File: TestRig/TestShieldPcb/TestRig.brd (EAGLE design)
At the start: 53.3 x 61 mm, 7 parts, among them J1 POWER_JACKPTH, U1 ARDUINO_SHIELDNOHOLES

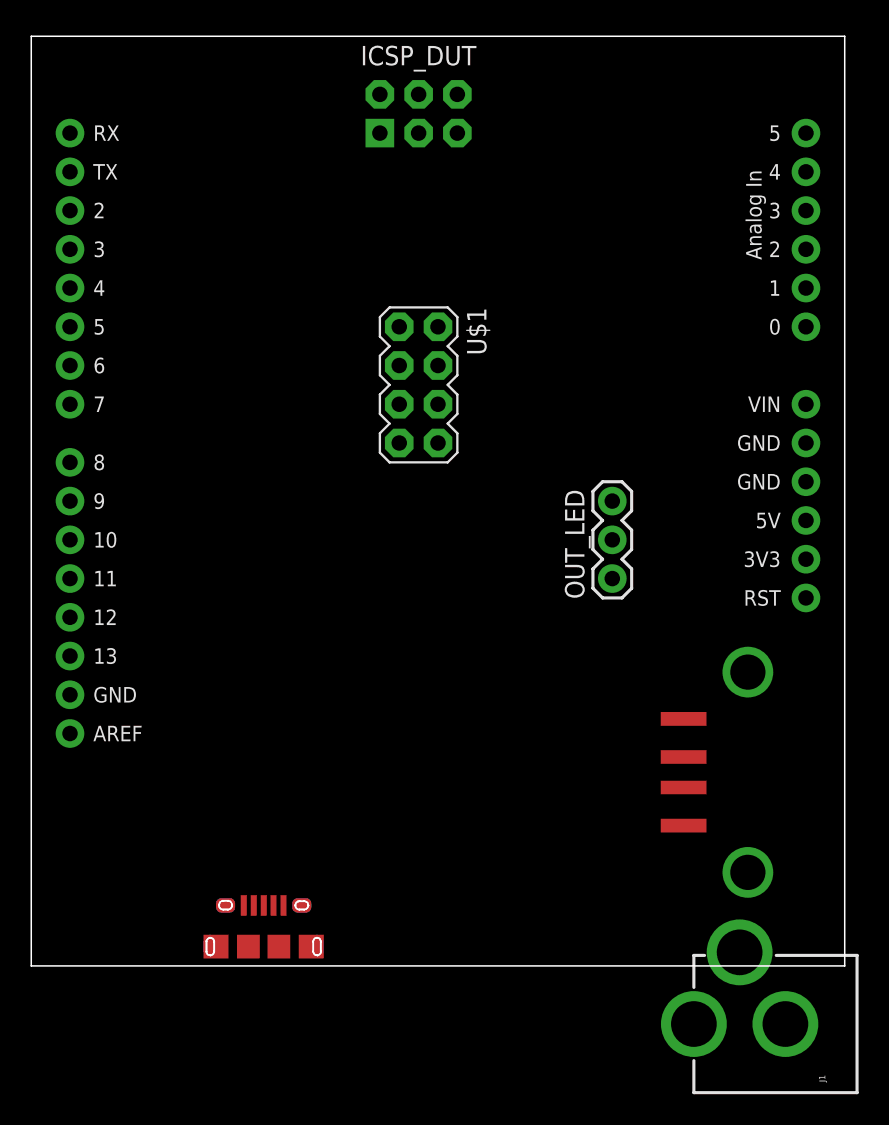
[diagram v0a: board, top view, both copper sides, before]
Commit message: Add test shield design
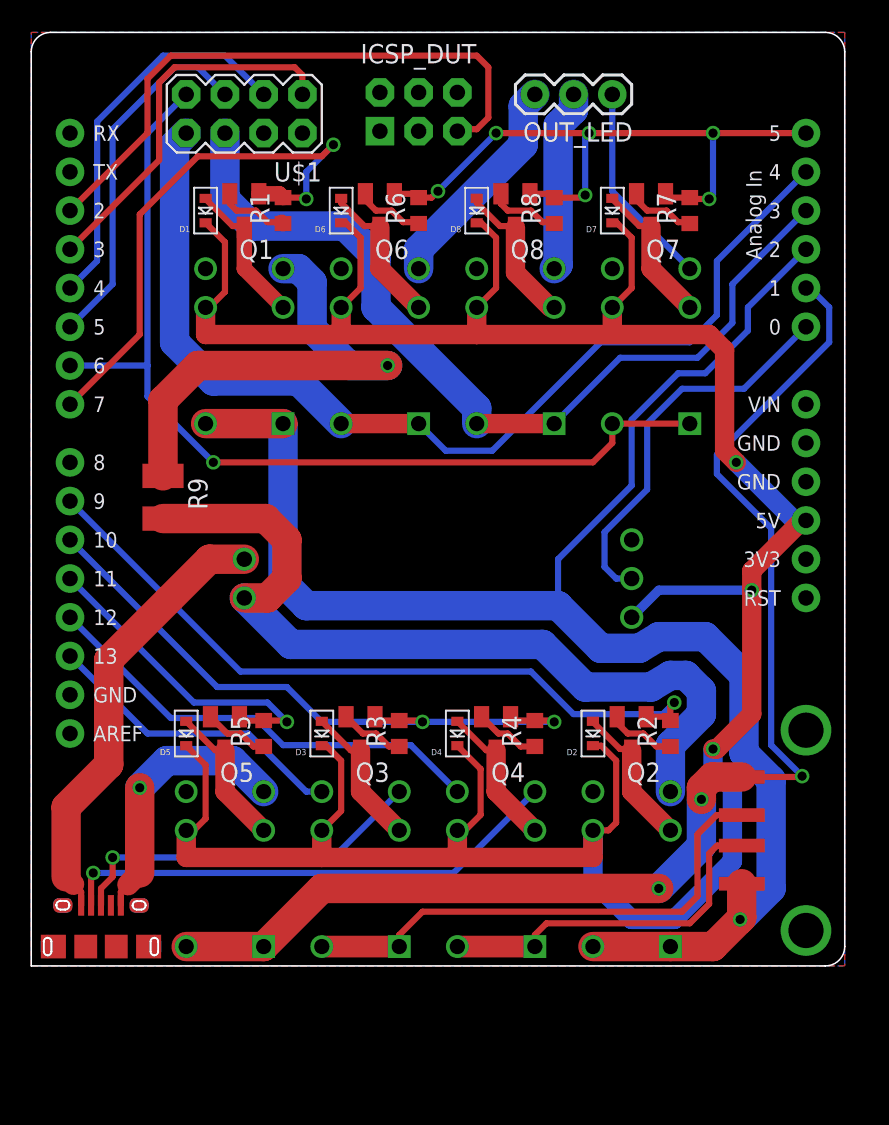
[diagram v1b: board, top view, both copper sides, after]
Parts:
- removed J1: POWER_JACKPTH, SparkFun-Connectors:POWER_JACK_PTH
- added D1, D2, D3, D4, D5, D6, D7, D8: (no value), adafruit:SOD-523
- added Q1, Q2, Q3, Q4, Q5, Q6, Q7, Q8: (no value), adafruit:SOT23
- added R1, R2, R3, R4, R5, R6, R7, R8: 1k, adafruit:R0603
- added R9: 25, adafruit:R1210
- added U$10, U$3, U$4, U$5, U$6, U$7, U$8, U$9: RELAY, blinkiverse:RELAY_HK23F-5V
- added U$11: SPARKFUN_ACS712, blinkiverse:SPARKFUN_ACS712
- moved OUT_LED 31.8 mm to (38.1, 57.1), turned to 180 degrees
- moved U$1 21.1 mm to (14.0, 55.9), turned to 180 degrees
- moved U$2 10.7 mm to (4.57, 1.27)
- moved JP1 5.39 mm to (50.8, 8.89)
- moved ICSP_DUT 0.13 mm to (25.4, 56.0)
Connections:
- net DUT_GND_IN renamed DUT_IN_GND_NC
- net DUT_VCC_IN renamed DUT_IN_VCC_NC
- removed net DUT_5V_OUT: U$1.6
- removed net DUT_GND_OUT: U$1.8
- removed net DUT_USB_V+: JP1.VBUS, U1.D12
- removed net N$1: U1.D4
- removed net N$10: U1.D9
- removed net N$2: U1.D5
- removed net N$7: U1.D6
- removed net N$8: U1.D7
- new net 5V: D1.K, D2.K, D3.K, D4.K, D5.K, D6.K, D7.K, D8.K, U$10.P$5, U$11.5V, U$3.P$5, U$4.P$5, U$5.P$5, U$6.P$5, U$7.P$5, U$8.P$5, U$9.P$5, U1.5V
- new net DUT_CURRENT: U$11.VOUT, U1.A0
- new net DUT_OUT_GND: U$1.8, U$8.P$1, U$8.P$6, U1.A4
- new net DUT_OUT_VCC: U$1.6, U$9.P$1, U$9.P$6, U1.A3
- new net DUT_USB_VCC: JP1.VBUS, U$3.P$1, U$3.P$6, U$7.P$1, U$7.P$6, U1.A2
- new net EN_LED_OUT: Q6.1, Q7.1, Q8.1, R6.2, R7.2, R8.2, U1.A5
- new net EN_USB_DATA: Q3.1, Q4.1, R3.2, R4.2, U1.D10
- new net EN_USB_GND: Q5.1, R5.2, U1.D11
- new net EN_USB_VCC: Q2.1, R2.2, U1.D9
- new net EN_USB_VCC_LIMIT: Q1.1, R1.2, U1.D7
- new net GND: Q1.2, Q2.2, Q3.2, Q4.2, Q5.2, Q6.2, Q7.2, Q8.2, R1.1, R2.1, R3.1, R4.1, R5.1, R6.1, R7.1, R8.1, U$11.GND, U1.GND@0, U1.GND@1
- new net HOST_USB_D+: U$2.PIN$3, U$4.P$3
- new net HOST_USB_D-: U$2.PIN$2, U$5.P$3
- new net HOST_USB_GND: U$2.PIN$5, U$6.P$3
- new net HOST_USB_VCC: U$11.IP+, U$2.PIN$1
- new net HOST_USB_VCC_M: R9.2, U$11.IP-, U$3.P$3
- new net LED_OUT_GND: OUT_LED.3, U$8.P$3
- new net LED_OUT_SIG: OUT_LED.1, U$10.P$3
- new net LED_OUT_VCC: OUT_LED.2, U$9.P$3
- new net N$14: D1.A, Q1.3, U$7.P$2
- new net N$20: D2.A, Q2.3, U$3.P$2
- new net N$27: D3.A, Q3.3, U$4.P$2
- new net N$31: D4.A, Q4.3, U$5.P$2
- new net N$35: D5.A, Q5.3, U$6.P$2
- new net N$38: D6.A, Q6.3, U$8.P$2
- new net N$42: D7.A, Q7.3, U$10.P$2
- new net N$46: D8.A, Q8.3, U$9.P$2
- new net TAP_USB_D+: U$4.P$4, U1.D13
- new net TAP_USB_D-: U$5.P$4, U1.D12
- net DUT_A10: now also U1.D3
- net DUT_D11: now also U1.D4
- net DUT_D13: now also U$10.P$1, U$10.P$6, U1.D6
- net DUT_D7: now also U1.D5
- net DUT_USB_D+: now also U$4.P$1, U$4.P$6; no longer U1.D10
- net DUT_USB_D-: now also U$5.P$1, U$5.P$6; no longer U1.D11
- net DUT_USB_GND: now also U$6.P$1, U$6.P$6, U1.A1; no longer U1.D13
- net ICSP_RESET: now also U1.D2
- net N$9: now also R9.1, U$7.P$3; no longer U1.D8
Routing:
- net 5V: track 0.00 -> 194.2 mm, vias 0 -> 3
- net DUT_USB_VCC: track 0.00 -> 110.3 mm, vias 0 -> 1
- net DUT_USB_GND: track 0.00 -> 85.4 mm, vias 0 -> 3
- net DUT_OUT_GND: track 0.00 -> 68.0 mm
- net DUT_D13: track 0.00 -> 65.1 mm, vias 0 -> 1
- net DUT_OUT_VCC: track 0.00 -> 58.3 mm
- net HOST_USB_VCC_M: track 0.00 -> 55.0 mm
- net EN_USB_VCC: track 0.00 -> 48.7 mm, vias 0 -> 1
- net EN_LED_OUT: track 0.00 -> 44.2 mm, vias 0 -> 6
- net EN_USB_DATA: track 0.00 -> 42.9 mm, vias 0 -> 2
- net ICSP_RESET: track 0.00 -> 39.7 mm
- net EN_USB_VCC_LIMIT: track 0.00 -> 36.5 mm, vias 0 -> 2
- net GND: track 0.00 -> 35.2 mm
- net DUT_USB_D+: track 0.00 -> 33.9 mm
- net HOST_USB_D-: track 0.00 -> 33.4 mm, vias 0 -> 1
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- added copper zone on layer 1, net GND
- added copper zone on layer 16, net GND
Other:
- board size 53.3 x 61 mm -> 53.3 x 61.2 mm

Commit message: RevD of the test shield PCB
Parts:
- removed JP1: USB-A-SMD, SparkFun-Connectors:USB-A-S-NOSILK-FEMALE
- added TEST_DUT: M04X2, SparkFun-Connectors:2X4
- added U$12: (no value), blinkiverse:OSHW-LOGO-L
- U$1: value M04X2 -> USB; device SparkFun-Connectors:2X4 -> blinkiverse:USB_A_FEMALE_NOSILK_SHIELD
- moved U$1 59.7 mm to (50.8, 8.89)
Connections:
- new net DUT_USB_SHIELD: U$1.SHIELD1, U$1.SHIELD2, U1.D7
- net DUT_A10: now also TEST_DUT.1; no longer U$1.1
- net DUT_D11: now also TEST_DUT.3; no longer U$1.3
- net DUT_D13: now also TEST_DUT.7; no longer U$1.7
- net DUT_D7: now also TEST_DUT.5; no longer U$1.5
- net DUT_IN_GND_NC: now also TEST_DUT.4; no longer U$1.4
- net DUT_IN_VCC_NC: now also TEST_DUT.2; no longer U$1.2
- net DUT_OUT_GND: now also TEST_DUT.8; no longer U$1.8
- net DUT_OUT_VCC: now also TEST_DUT.6; no longer U$1.6
- net DUT_USB_D+: now also U$1.D+; no longer JP1.D+
- net DUT_USB_D-: now also U$1.D-; no longer JP1.D-
- net DUT_USB_GND: now also U$1.GND; no longer JP1.GND
- net DUT_USB_VCC: now also U$1.VBUS; no longer JP1.VBUS
- net EN_USB_VCC_LIMIT: now also U1.D8; no longer U1.D7
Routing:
- net DUT_USB_SHIELD: track 0.00 -> 87.0 mm, vias 0 -> 2
- net DUT_USB_VCC: track 110.3 -> 101.8 mm
- net EN_USB_VCC_LIMIT: track 36.5 -> 41.9 mm
- net DUT_USB_GND: track 85.4 -> 81.6 mm
- net DUT_USB_D+: track 33.9 -> 31.6 mm
- net DUT_USB_D-: track 23.8 -> 21.8 mm
- net 5V: track 194.2 -> 195.6 mm
- net HOST_USB_VCC_M: track 55.0 -> 55.3 mm, vias 0 -> 1
- net GND: vias 0 -> 20
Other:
- board text added: "5V"
- board text added: "BlinkyTape Test Shield"
- board text added: "DUT USB"
- board text added: "GND"
- board text added: "HOST USB"
- board text added: "OGND"
- board text added: "OUT_LED"
- board text added: "OVCC"
- board text added: "RevD, 06/13"
- board text added: "SIG"
- board text added: "TEST_DUT"
- board text added: "_A10"
- board text added: "_D11"
- board text added: "_D13"
- board text added: "_D7"

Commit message: Minor updates to test rig
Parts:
- moved U$12 13.7 mm to (8.26, 21.3), turned to 90 degrees
- moved OUT_LED 3.81 mm to (41.9, 57.1)
- moved TEST_DUT 3.18 mm to (10.8, 55.9)
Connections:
- net HOST_USB_VCC: now also U$11.IP-; no longer U$11.IP+
- net HOST_USB_VCC_M: now also U$11.IP+; no longer U$11.IP-
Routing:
- net ICSP_RESET: track 39.7 -> 44.6 mm
- net HOST_USB_VCC_M: track 55.3 -> 50.8 mm
- net HOST_USB_VCC: track 29.3 -> 26.7 mm
- net LED_OUT_GND: track 14.6 -> 16.9 mm
- net EN_LED_OUT: track 44.2 -> 45.8 mm
- net LED_OUT_VCC: track 12.0 -> 13.5 mm
- net LED_OUT_SIG: track 13.5 -> 12.0 mm
- net DUT_D11: track 25.4 -> 26.8 mm
- net DUT_OUT_VCC: track 58.3 -> 59.5 mm
- net DUT_D7: track 23.9 -> 23.0 mm
- net DUT_D13: track 65.1 -> 64.3 mm
- net DUT_A10: track 24.6 -> 23.8 mm
- net DUT_OUT_GND: track 68.0 -> 68.7 mm
- net GND: vias 20 -> 21
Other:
- board text added: "RevD.1, 07/13"
- board text removed: "RevD, 06/13"

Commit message: Test rig update: programming, current measurement functional
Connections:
- net DUT_A10: now also U1.TX; no longer U1.D3
- net ICSP_RESET: now also U1.RX; no longer U1.D2
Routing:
- net ICSP_RESET: track 44.6 -> 38.2 mm
- net DUT_A10: track 23.8 -> 18.8 mm
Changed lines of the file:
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@@
 <signal name="ICSP_RESET">
 <contactref element="ICSP_DUT" pad="5"/>
-<contactref element="U1" pad="D2"/>
-<wire x1="2.54" y1="49.53" x2="1.016" y2="51.054" width="0.4064" layer="1"/>
-<wire x1="1.016" y1="51.054" x2="1.016" y2="57.658" width="0.4064" layer="1"/>
-<wire x1="1.016" y1="57.658" x2="3.048" y2="59.69" width="0.4064" layer="1"/>
 <wire x1="3.048" y1="59.69" x2="29.21" y2="59.69" width="0.4064" layer="1"/>
 <wire x1="29.21" y1="59.69" x2="29.972" y2="58.928" width="0.4064" layer="1"/>
@@
 <wire x1="29.21" y1="54.864" x2="28.067" y2="54.864" width="0.4064" layer="1"/>
 <wire x1="28.067" y1="54.864" x2="27.94" y2="54.737" width="0.4064" layer="1"/>
+<contactref element="U1" pad="RX"/>
+<wire x1="2.54" y1="54.61" x2="2.54" y2="59.182" width="0.4064" layer="1"/>
+<wire x1="2.54" y1="59.182" x2="3.048" y2="59.69" width="0.4064" layer="1"/>
 </signal>
 <signal name="DUT_A10">
 <contactref element="TEST_DUT" pad="1"/>
-<contactref element="U1" pad="D3"/>
-<wire x1="2.54" y1="46.99" x2="4.318" y2="48.768" width="0.4064" layer="1"/>
-<wire x1="4.318" y1="48.768" x2="4.318" y2="57.912" width="0.4064" layer="1"/>
 <wire x1="4.318" y1="57.912" x2="5.334" y2="58.928" width="0.4064" layer="1"/>
 <wire x1="5.334" y1="58.928" x2="14.097" y2="58.928" width="0.4064" layer="1"/>
 <wire x1="14.097" y1="58.928" x2="14.605" y2="58.42" width="0.4064" layer="1"/>
 <wire x1="14.605" y1="58.42" x2="14.605" y2="57.15" width="0.4064" layer="1"/>
+<contactref element="U1" pad="TX"/>
+<wire x1="4.318" y1="57.912" x2="4.318" y2="53.848" width="0.4064" layer="1"/>
+<wire x1="4.318" y1="53.848" x2="2.54" y2="52.07" width="0.4064" layer="1"/>
 </signal>
 <signal name="DUT_D11">
@@
 </signal>
 </signals>
-<errors>
-</errors>
 </board>
 </drawing>
